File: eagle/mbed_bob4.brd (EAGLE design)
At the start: 50 x 70 mm, 15 parts, among them IC1 MBED-SOCKET, K1 651005136521, K2 691210910006, K3 691210910006, T1 2N7002E

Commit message: First working version. To be cleaned up and checked before sending out for production.
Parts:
- added IC2: MAX9934, ic:UMAX8
- added K4: 691210910006, Wuerth_Elektronik_eiCan_14_Terminal_Blocks_WR-TBL_2_0:691210910006
- added R8: R_KELVIN, passives:R_KELVIN_1206
- added X1: SDCARDSHORT, connectors:SD_SHORT
- ETH1: value CON-RJ45-F -> CON-RJ45-F_WE100; device dp_devices:HR911105A -> connectors:74990111215A
- moved C1 17.6 mm to (27.9, 52.7), turned to 270 degrees
- moved RN2 9.16 mm to (21.6, 16.5), turned to 90 degrees
- moved R5 5.08 mm to (11.4, 10.2)
- moved R1 2.54 mm to (44.5, 15.2)
- moved T1 2.54 mm to (44.5, 10.2)
- moved R3 2.54 mm to (16.5, 10.2)
- moved R4 2.54 mm to (14.0, 10.2)
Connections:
- new net CAN_RX: IC1.30, IC1.30A, K4.1
- new net CAN_TX: IC1.29, IC1.29A, K4.2
- new net MAX_CS: IC1.22, IC1.22A, IC2.6
- new net N$14: IC1.7, IC1.7A, X1.5
- new net N$15: IC1.8, IC1.8A, X1.1
- new net N$16: IC1.5, IC1.5A, X1.2
- new net N$17: IC1.6, IC1.6A, X1.7
- new net N$18: IC1.VB, IC1.VBA
- new net N$19: IC1.NR, IC1.NRA
- new net N$20: IC1.11, IC1.11A
- new net N$21: IC1.12, IC1.12A
- new net N$22: IC1.13, IC1.13A
- new net N$23: IC1.15, IC1.15A
- new net N$24: IC1.16, IC1.16A, IC2.2
- new net N$25: K3.3, R8.I1
- new net N$26: IC1.23, IC1.23A
- new net N$27: IC1.24, IC1.24A
- new net N$28: IC1.IF+, IC1.IF+A
- new net N$29: IC1.IF-, IC1.IF-A
- new net N$30: IC1.VU, IC1.VUA
- new net N$31: IC2.7, R8.V2
- new net N$32: IC2.8, R8.V1
- new net N$33: K3.4, R8.I2
- new net PWM25: IC1.25, IC1.25A, K4.6
- new net PWM26: IC1.26, IC1.26A, K4.5
- new net SCL: IC1.27, IC1.27A, K4.4
- new net SDA: IC1.28, IC1.28A, K4.3
- net +3V3: now also ETH1.2, IC2.1, X1.4; no longer ETH1.4
- net GND: now also ETH1.12, ETH1.SH1, ETH1.SH2, IC2.3, RN2.1, RN2.2, RN2.3, RN2.4, X1.3, X1.6, X1.GND@1, X1.GND@2, X1.GND@3, X1.GND@4; no longer ETH1.11
- net LED1: now also IC1.9, IC1.9A
- net LED2: now also IC1.10, IC1.10A
- net N$1: now also RN2.5; no longer RN2.8
- net N$11: now also ETH1.11; no longer ETH1.12
- net N$3: now also IC1.14, IC1.14A, X1.10; no longer RN2.1, RN2.2, RN2.3, RN2.4
- net N$5: now also RN2.8; no longer RN2.5
- net N$6: now also RN2.7; no longer RN2.6
- net N$7: now also RN2.6; no longer RN2.7
- net RX_P: now also ETH1.4; no longer ETH1.3
- net TX_N: now also ETH1.3; no longer ETH1.2
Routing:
- net +3V3: track 0.00 -> 171.0 mm, vias 0 -> 1
- net VBUS: track 0.00 -> 59.2 mm
- net USB_D_P: track 0.00 -> 36.1 mm, vias 0 -> 1
- net USB_D_N: track 0.00 -> 35.5 mm
- net LED2: track 0.00 -> 35.3 mm
- net LED1: track 0.00 -> 34.0 mm
- net N$17: track 0.00 -> 29.5 mm, vias 0 -> 1
- net TX_P: track 0.00 -> 27.5 mm
- net TX_N: track 0.00 -> 25.4 mm
- net N$11: track 0.00 -> 21.6 mm
- net N$1: track 0.00 -> 21.0 mm
- net N$7: track 0.00 -> 19.9 mm, vias 0 -> 1
- net N$14: track 0.00 -> 19.4 mm
- net N$6: track 0.00 -> 19.4 mm, vias 0 -> 1
- net N$5: track 0.00 -> 18.6 mm, vias 0 -> 1
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- added copper zone on layer 1, net GND
- added copper zone on layer 16, net GND

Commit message: Further cleanup
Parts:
- renumbered K1 to USB
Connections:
- removed net N$2: USB.5
- net +3V3: now also K3.1
- net GND: now also USB.5
- net N$13: now also K3.4
- net N$25: now also K3.2; no longer K3.3
- net N$33: now also K3.3; no longer K3.4
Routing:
- net N$24: track 2.54 -> 32.3 mm
- net LGC_IN_LV: track 2.54 -> 16.8 mm, vias 0 -> 1
- net +3V3: track 171.0 -> 183.6 mm
- net MAX_CS: track 2.54 -> 12.6 mm, vias 0 -> 1
- net N$25: track 0.00 -> 7.27 mm
- net N$33: track 0.00 -> 7.27 mm
- net GND: track 7.97 -> 10.8 mm, vias 21 -> 35
- net N$13: track 6.69 -> 8.37 mm
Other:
- board text added: "CAN"
- board text added: "PWM5"
- board text added: "PWM6"
- board text added: "RX"
- board text added: "SCL"
- board text added: "SDA"
- board text added: "SRX"
- board text added: "STX"
- board text added: "TX"
- board text added: "likatronix.be"
- board text added: "mbed-bob4 v1"

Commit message: Final version before boardout.
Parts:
- added C2, R10, R9: (no value), passives:0805_RFLW
- moved T1 1.90 mm to (44.5, 12.1)
- moved R1 1.27 mm to (44.5, 16.5)
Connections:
- net GND: now also C2.P$3, R10.P$3, R9.P$3
- net N$13: now also R10.P$4
- net N$24: now also C2.P$4, R9.P$4
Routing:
- net N$13: track 8.37 -> 11.7 mm
- net GND: track 10.8 -> 12.6 mm, vias 35 -> 41
- net +3V3: track 183.6 -> 182.4 mm
- net LGC_IN_LV: track 16.8 -> 18.0 mm
- net N$24: track 32.3 -> 33.0 mm
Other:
- board text added: "BTM"
- board text added: "TOP"

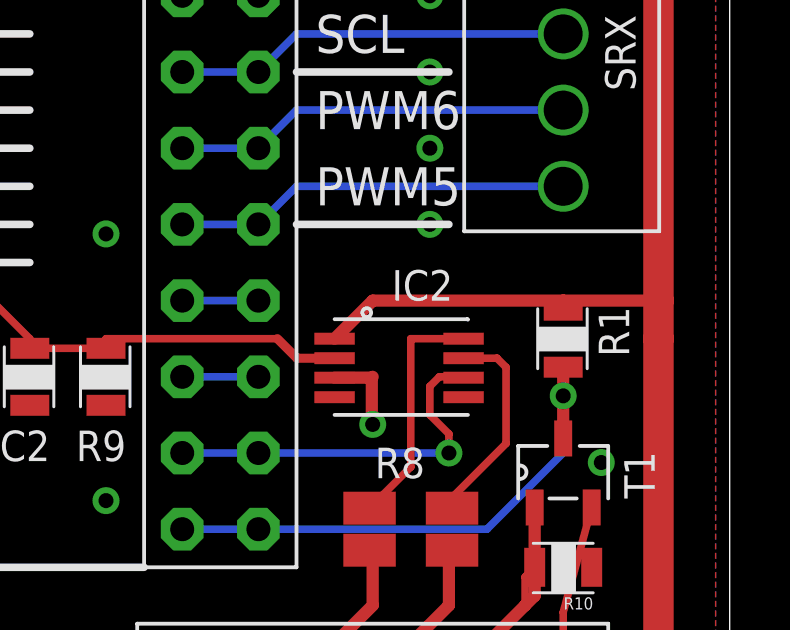
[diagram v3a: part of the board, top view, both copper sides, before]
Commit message: Added decoupling resistor.
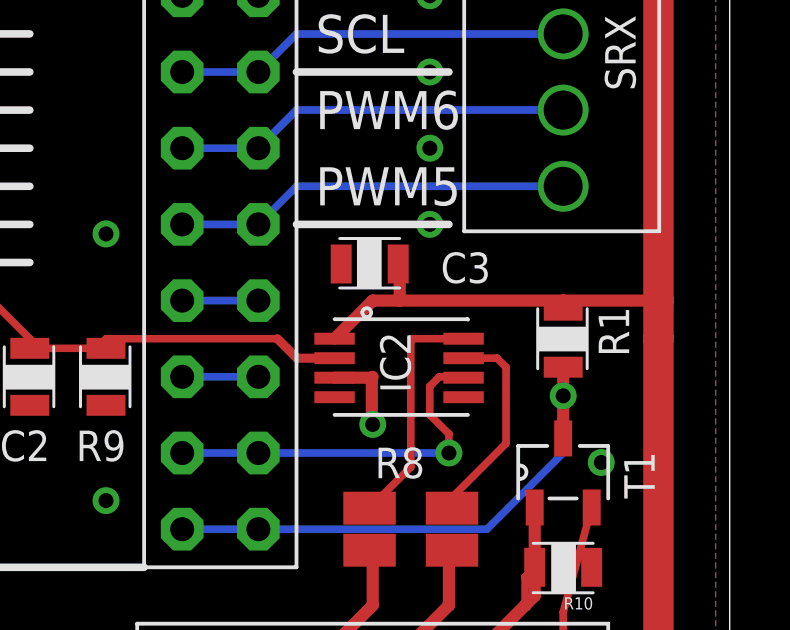
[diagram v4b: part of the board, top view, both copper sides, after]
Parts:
- added C3: (no value), passives:0805_RFLW
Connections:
- net +3V3: now also C3.P$4
- net GND: now also C3.P$3
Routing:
- net +3V3: track 182.4 -> 183.6 mm
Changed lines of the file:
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@@
 <setting verticaltext="up"/>
 </settings>
-<grid distance="1.27" unitdist="mm" unit="mm" style="lines" multiple="1" display="yes" altdistance="0.635" altunitdist="mm" altunit="mm"/>
+<grid distance="1" unitdist="mm" unit="mm" style="lines" multiple="1" display="yes" altdistance="0.635" altunitdist="mm" altunit="mm"/>
 <layers>
 <layer number="1" name="Top" color="4" fill="1" visible="yes" active="yes"/>
@@
 <layer number="45" name="Holes" color="7" fill="1" visible="no" active="yes"/>
 <layer number="46" name="Milling" color="3" fill="1" visible="no" active="yes"/>
-<layer number="47" name="Measures" color="7" fill="1" visible="no" active="yes"/>
+<layer number="47" name="Measures" color="7" fill="1" visible="yes" active="yes"/>
 <layer number="48" name="Document" color="7" fill="1" visible="no" active="yes"/>
 <layer number="49" name="Reference" color="7" fill="1" visible="no" active="yes"/>
@@
 <text x="22.86" y="33.02" size="1.778" layer="1" ratio="15">TOP</text>
 <text x="27.94" y="33.02" size="1.778" layer="16" ratio="15" rot="MR0">BTM</text>
+<dimension x1="0" y1="70" x2="50" y2="70" x3="25" y3="74" textsize="1.778" layer="47"/>
+<dimension x1="50" y1="0" x2="50" y2="70" x3="54" y3="35" textsize="1.778" layer="47"/>
 </plain>
 <attributes>
@@
 <attribute name="MPN" value="MAX9934" x="36.83" y="16.51" size="1.778" layer="27" display="off"/>
 <attribute name="MF" value="Maxim" x="36.83" y="16.51" size="1.778" layer="27" display="off"/>
-<attribute name="NAME" x="38.735" y="17.78" size="1.016" layer="25"/>
+<attribute name="NAME" x="39.37" y="14.7" size="1.016" layer="25" rot="R90"/>
 </element>
 <element name="R9" library="passives" package="0805_RFLW" value="" x="29.21" y="15.24" smashed="yes" rot="R90">
@@
 </element>
 <element name="R10" library="passives" package="0805_RFLW" value="" x="44.45" y="8.89" rot="R180"/>
+<element name="C3" library="passives" package="0805_RFLW" value="" x="38" y="19" smashed="yes">
+<attribute name="NAME" x="40.365" y="18.365" size="1.016" layer="25" font="vector"/>
+<attribute name="VALUE" x="37" y="17.6" size="0.4064" layer="27" font="vector"/>
+</element>
 </elements>
 <signals>
@@
 <via x="46.99" y="60.96" extent="1-16" drill="0.5"/>
 <via x="48.26" y="1.27" extent="1-16" drill="0.5"/>
+<contactref element="C3" pad="P$3"/>
 </signal>
 <signal name="+3V3">
@@
 <contactref element="K3" pad="1"/>
 <wire x1="36.83" y1="16.51" x2="38.1" y2="17.78" width="0.4064" layer="1"/>
-<wire x1="38.1" y1="17.78" x2="44.45" y2="17.78" width="0.4064" layer="1"/>
+<wire x1="38.1" y1="17.78" x2="39" y2="17.78" width="0.4064" layer="1"/>
+<wire x1="39" y1="17.78" x2="44.45" y2="17.78" width="0.4064" layer="1"/>
 <wire x1="44.45" y1="17.78" x2="47.625" y2="17.78" width="0.4064" layer="1"/>
 <wire x1="44.45" y1="17.46" x2="44.45" y2="17.78" width="0.4064" layer="1"/>
 <wire x1="31.75" y1="3.81" x2="31.75" y2="1.27" width="0.6096" layer="1"/>
+<contactref element="C3" pad="P$4"/>
+<wire x1="38.95" y1="19" x2="39" y2="19" width="0.4064" layer="1"/>
+<wire x1="39" y1="19" x2="39" y2="17.78" width="0.4064" layer="1"/>
 </signal>
 <signal name="LGC_IN_LV">
